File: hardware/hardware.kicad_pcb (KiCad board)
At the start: 2 copper layers, 22 parts, among them J1 Screw_Terminal_01x02, J2 Screw_Terminal_01x02, J3 Screw_Terminal_01x02, K1 RM85-2011-35-1005, K2 RM85-2011-35-1005, Q1 BC337, Q2 BC337, U1 XIAO-ESP32-C6, U2 DS18B20

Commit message: Started working on PCB
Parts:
- removed D3, D4: LED, LED_THT:LED_D5.0mm
- removed R7, R8: 100R, Resistor_THT:R_Axial_DIN0204_L3.6mm_D1.6mm_P7.62mm_Horizontal
- D1, D2: footprint Diode_THT:D_DO-41_SOD81_P10.16mm_Horizontal -> Diode_THT:D_A-405_P7.62mm_Horizontal
- moved R4 55.7 mm to (115.5, 46.2), turned to -90 degrees
- moved R2 55.4 mm to (118.5, 53.8), turned to 90 degrees
- moved R6 52.4 mm to (112.5, 53.8), turned to 90 degrees
- moved R5 51.4 mm to (109.5, 46.2), turned to -90 degrees
- moved K1 49.4 mm to (94.5, 44.5), turned to 90 degrees
- moved U2 48.9 mm to (110.1, 36.2), turned to -90 degrees
- moved U1 46.5 mm to (110.5, 66.7), turned to -90 degrees
- moved PS1 40.2 mm to (45.1, 41.5), turned to -90 degrees
- moved J2 36.2 mm to (93.0, 32.3), turned to 180 degrees
- moved Q2 34.2 mm to (103.1, 45.2), turned to -90 degrees
- moved K2 33.5 mm to (79.0, 44.5), turned to 90 degrees
- moved R1 29.7 mm to (87.2, 74.0)
- moved Q1 29.4 mm to (103.1, 51.7), turned to -90 degrees
- moved J3 25.3 mm to (78.0, 32.3), turned to 180 degrees
- moved D1 20.8 mm to (94.8, 70.5), turned to 180 degrees
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
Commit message: Improved PCB layout
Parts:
- moved Q2 49.4 mm to (55.5, 58.4)
- moved R5 33.8 mm to (75.9, 42.3), turned to 0 degrees
- moved Q1 32.3 mm to (71.5, 58.4)
- moved R6 32.2 mm to (83.5, 39.7), turned to 180 degrees
- moved U2 31.2 mm to (79.0, 35.2), turned to 180 degrees
- moved R3 30.3 mm to (44.0, 61.7)
- moved D2 30.0 mm to (51.8, 58.6)
- moved R1 29.8 mm to (60.0, 61.7)
- moved J3 29.8 mm to (50.8, 20.1)
- moved D1 29.5 mm to (67.8, 58.6)
- moved J2 28.9 mm to (66.8, 20.1)
- moved R4 28.3 mm to (87.5, 42.3), turned to 0 degrees
- moved U1 28.0 mm to (85.4, 54.1)
- moved PS1 27.8 mm to (20.1, 29.3)
- moved K2 27.7 mm to (54.1, 32.3)
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
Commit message: Started working on new PCB layout
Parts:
- moved Q2 101.5 mm to (156.7, 66.5), turned to 0 degrees
- moved R3 96.9 mm to (132.8, 100.5)
- moved U2 92.5 mm to (156.9, 85.0), turned to 0 degrees
- moved R5 86.0 mm to (132.8, 106.8)
- moved R6 85.9 mm to (132.8, 110.0), turned to 0 degrees
- moved Q1 85.3 mm to (156.7, 60.7), turned to 0 degrees
- moved R4 76.3 mm to (132.8, 103.7)
- moved U1 73.9 mm to (157.6, 38.1), turned to 0 degrees
- moved R2 68.9 mm to (132.8, 97.4), turned to 0 degrees
- moved J2 19.6 mm to (47.2, 19.4), turned to 0 degrees
- moved D2 17.6 mm to (69.4, 59.9)
- moved K1 16.7 mm to (53.5, 33.0)
- moved K2 15.1 mm to (69.2, 33.0)
- moved R1 14.6 mm to (45.5, 63.7)
- moved D1 14.5 mm to (53.4, 59.7)
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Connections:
- J2 pad 1: unconnected-(J2-Pin_1-Pad1) -> RELAY_A_IN
- J2 pad 2: unconnected-(J2-Pin_2-Pad2) -> RELAY_A_OUT
- J3 pad 1: unconnected-(J3-Pin_1-Pad1) -> RELAY_B_IN
- J3 pad 2: unconnected-(J3-Pin_2-Pad2) -> RELAY_B_OUT
- K1 pad 11: unconnected-(K1-COM_1-Pad11) -> RELAY_A_IN
- K1 pad 14: unconnected-(K1-NO_1-Pad14) -> RELAY_A_OUT
- K1 pad 21: unconnected-(K1-COM_2-Pad21) -> RELAY_A_IN
- K1 pad 24: unconnected-(K1-NO_2-Pad24) -> RELAY_A_OUT
- K2 pad 11: unconnected-(K2-COM_1-Pad11) -> RELAY_B_IN
- K2 pad 14: unconnected-(K2-NO_1-Pad14) -> RELAY_B_OUT
- K2 pad 21: unconnected-(K2-COM_2-Pad21) -> RELAY_B_IN
- K2 pad 24: unconnected-(K2-NO_2-Pad24) -> RELAY_B_OUT
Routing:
- net RELAY_A_IN: track 0.00 -> 29.9 mm
- net RELAY_B_IN: track 0.00 -> 29.8 mm
- net 230VAC_N: track 0.00 -> 20.1 mm
- net 230VAC_L: track 0.00 -> 17.5 mm
- net RELAY_B_OUT: track 0.00 -> 16.6 mm
- net RELAY_A_OUT: track 0.00 -> 16.6 mm

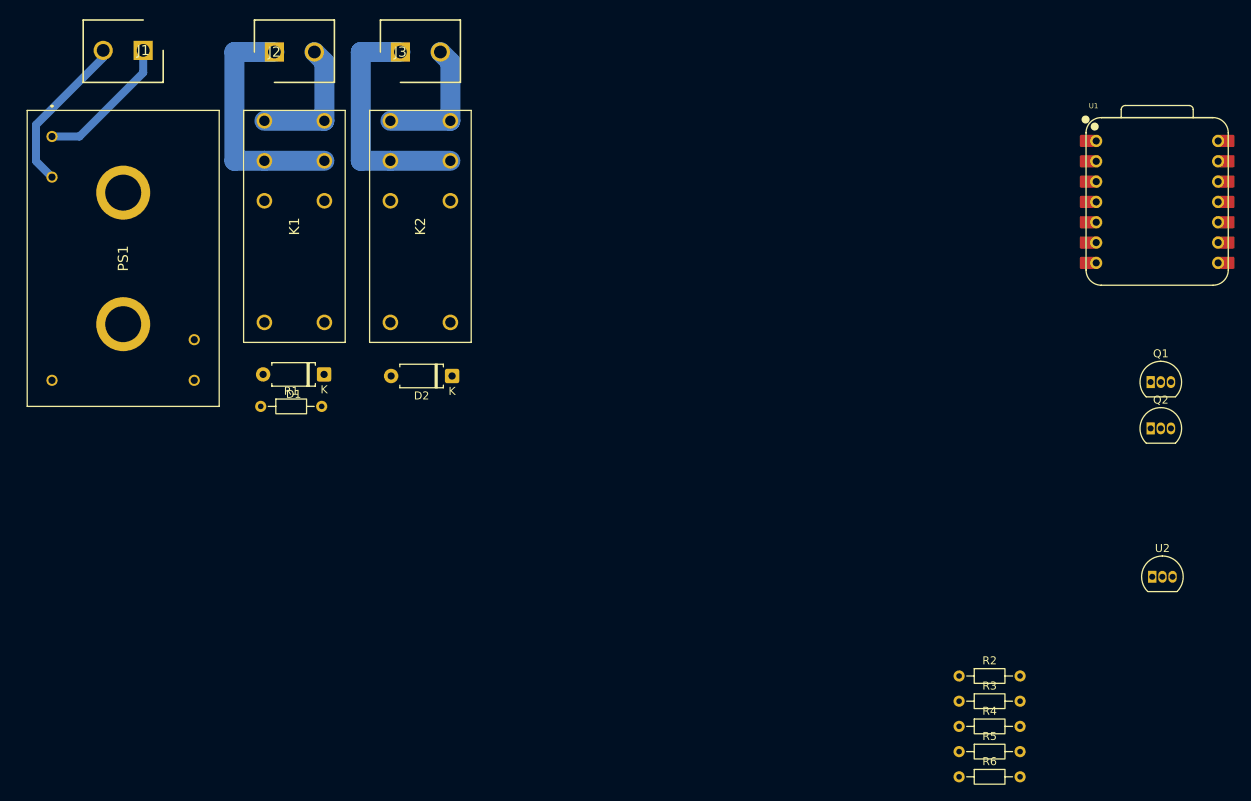
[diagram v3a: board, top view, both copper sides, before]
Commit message: New layout with new screw terminals
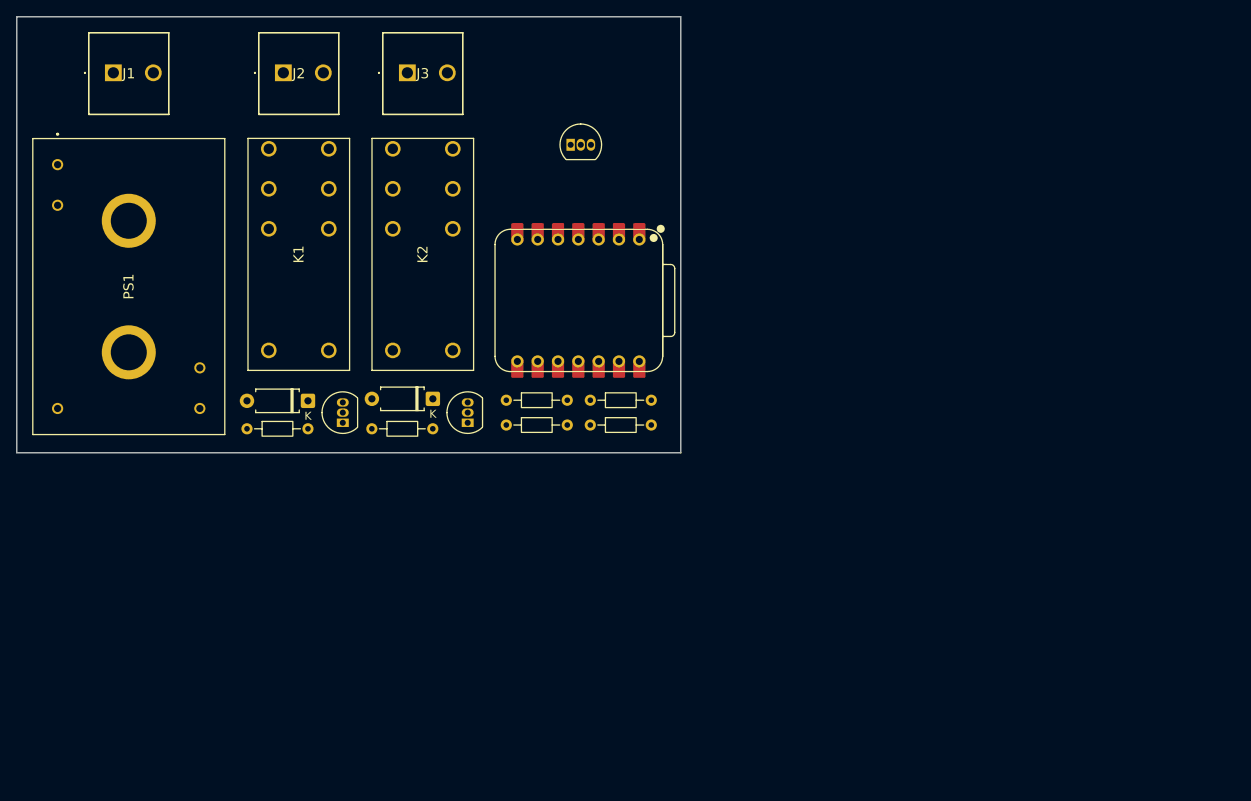
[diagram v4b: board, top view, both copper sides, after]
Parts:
- J1, J2, J3: footprint Degson Electronics:SHDR2W100P0X500_1X2_1000X780X1020P -> Degson Electronics:DG1285002P14
- moved Q1 101.1 mm to (55.8, 65.7), turned to 90 degrees
- moved U2 90.6 mm to (84.2, 31.0)
- moved Q2 85.4 mm to (71.4, 65.7), turned to 90 degrees
- moved R3 80.9 mm to (59.4, 66.5)
- moved U1 73.4 mm to (85.2, 50.5), turned to -90 degrees
- moved R5 69.8 mm to (76.2, 66.0)
- moved R4 69.8 mm to (76.2, 62.9)
- moved R6 63.7 mm to (86.7, 66.0)
- moved R2 57.6 mm to (86.7, 62.9)
- moved J1 4.66 mm to (27.1, 22.0), turned to 0 degrees
- moved D1 3.87 mm to (51.4, 63.0)
- moved D2 3.73 mm to (67.0, 62.8)
- moved PS1 3.59 mm to (20.1, 33.5)
- moved K1 3.54 mm to (54.0, 36.5)
- moved K2 3.51 mm to (69.5, 36.5)
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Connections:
- U1 pad 1: RELAY_A_CTRL -> unconnected-(U1-GPIO0/A0/D0-Pad1)
- U1 pad 10: unconnected-(U1-GPIO20/D9/MISO-Pad10) -> RELAY_A_CTRL
- U1 pad 2: RELAY_B_CTRL -> unconnected-(U1-GPIO1/A1/D1-Pad2)
- U1 pad 3: LED_A -> TEMP_SENSOR_DATA
- U1 pad 4: LED_B -> unconnected-(U1-GPIO21/D3-Pad4)
- U1 pad 5: TEMP_SENSOR_DATA -> unconnected-(U1-GPIO22/D4/SDA-Pad5)
- U1 pad 9: unconnected-(U1-GPIO19/D8/SCK-Pad9) -> RELAY_B_CTRL
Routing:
- net RELAY_A_IN: track 29.9 -> 0.00 mm
- net RELAY_B_IN: track 29.8 -> 0.00 mm
- net 230VAC_N: track 20.1 -> 0.00 mm
- net 230VAC_L: track 17.5 -> 0.00 mm
- net RELAY_B_OUT: track 16.6 -> 0.00 mm
- net RELAY_A_OUT: track 16.6 -> 0.00 mm
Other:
- board outline added: 83 x 54.5 mm
